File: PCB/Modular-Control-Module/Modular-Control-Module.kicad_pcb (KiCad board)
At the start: 4 copper layers, 59 x 49.4 mm, 29 parts, among them J1 Conn_01x04, SW1 TL3330AF260QG, SW2 TL3330AF260QG, U1 TEMPLATE, U2 RP2040, X1 ABM8G-12.000MHZ-18-D2Y-T

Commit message: WIP save
WIP save gonna try flipping the MCU around.
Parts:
- added J2: DX07S016JA1R1500, AVR-KiCAD-Lib-Connectors:JAE_DX07S016JA1R1500, B.Cu at (82.8, 74.1)
- added R1: RT0603BRD071ML, AVR-KiCAD-Lib-Resistors:R0603, B.Cu at (79.0, 68.1)
- added R10: RC0402FR-071KL, AVR-KiCAD-Lib-Resistors:R0402, B.Cu at (88.5, 80.0)
- added R11: RC0402FR-071KL, AVR-KiCAD-Lib-Resistors:R0402, B.Cu at (106.9, 80.0)
- added R12: RC0402FR-071KL, AVR-KiCAD-Lib-Resistors:R0402, B.Cu at (125.5, 80.0)
- added R4: RC0402FR-075K1L, AVR-KiCAD-Lib-Resistors:R0402, B.Cu at (86.0, 72.8)
- added R5: RC0402FR-075K1L, AVR-KiCAD-Lib-Resistors:R0402, B.Cu at (87.4, 77.2)
- added R7: RC0402FR-071KL, AVR-KiCAD-Lib-Resistors:R0402, B.Cu at (125.5, 53.8)
- added R8: RC0402FR-071KL, AVR-KiCAD-Lib-Resistors:R0402, B.Cu at (107.0, 53.8)
- added R9: RC0402FR-071KL, AVR-KiCAD-Lib-Resistors:R0402, B.Cu at (88.5, 53.8)
- J1: value Conn_01x04 -> Conn_ARM_SWD_TagConnect_TC2030-NL; footprint Connector_PinHeader_2.54mm:PinHeader_1x04_P2.54mm_Vertical -> Connector:Tag-Connect_TC2030-IDC-NL_2x03_P1.27mm_Vertical; moved to B.Cu
- SW1, SW2: value TL3330AF260QG -> B3U-1000P; footprint AVR-KiCAD-Lib-Mech-Switches:SW_TL3330AF260QG -> AVR-KiCAD-Lib-Mech-Switches:B3U-1000P; moved to B.Cu
- moved J1 44.3 mm to (112.4, 75.8), turned to 180 degrees
- moved C14 28.4 mm to (98.2, 67.9), turned to -90 degrees
- moved C8 23.3 mm to (93.7, 69.0), turned to 0 degrees
- moved C11 18.4 mm to (88.0, 73.3), turned to 0 degrees
- moved SW2 16.8 mm to (79.2, 83.7)
- moved SW1 11.7 mm to (79.2, 64.0)
- moved C13 7.88 mm to (98.1, 80.2), turned to 90 degrees
- moved C7 5.85 mm to (92.9, 79.2)
- moved C6 2.91 mm to (90.4, 74.8)
- moved C3 2.28 mm to (91.8, 77.4)
- moved C4 2.11 mm to (107.9, 71.2), turned to 90 degrees
- moved X1 1.81 mm to (105.6, 71.8)
- moved C2 1.70 mm to (105.3, 74.5)
- moved C1 0.85 mm to (94.2, 79.3)
- moved C5 0.63 mm to (102.6, 75.0)
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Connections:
- EN2 pad 2: unconnected-(EN2-S2-Pad2) -> GND
- EN3 pad 2: unconnected-(EN3-S2-Pad2) -> GND
- EN6 pad 2: unconnected-(EN6-S2-Pad2) -> GND
- J1 pad 3: GND -> unconnected-(J1-~{RESET}-Pad3)
- U2 pad 12: unconnected-(U2-GPIO9-Pad12) -> /I2C_SDA
- U2 pad 13: unconnected-(U2-GPIO10-Pad13) -> /I2C_SCL
- U2 pad 14: unconnected-(U2-GPIO11-Pad14) -> /SLAVE_IRQ
- U2 pad 15: unconnected-(U2-GPIO12-Pad15) -> /SPI_SCK
- U2 pad 16: unconnected-(U2-GPIO13-Pad16) -> /SPI_CS
- U2 pad 17: unconnected-(U2-GPIO14-Pad17) -> /SPI_MISO
- U2 pad 18: unconnected-(U2-GPIO15-Pad18) -> /SPI_MOSI
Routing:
- net /SPI_MOSI: track 0.00 -> 33.4 mm, vias 0 -> 1
- net /SPI_MISO: track 0.00 -> 32.2 mm, vias 0 -> 1
- net /SPI_CS: track 0.00 -> 31.0 mm, vias 0 -> 1
- net /SPI_SCK: track 0.00 -> 30.2 mm, vias 0 -> 1
- net +3.3V: track 0.00 -> 27.7 mm, vias 0 -> 15
- net Net-(U2-RUN): track 0.00 -> 27.5 mm, vias 0 -> 2
- net /I2C_SDA: track 0.00 -> 26.1 mm, vias 0 -> 1
- net /SLAVE_IRQ: track 0.00 -> 25.9 mm, vias 0 -> 1
- net /I2C_SCL: track 0.00 -> 25.8 mm, vias 0 -> 1
- net /SWD: track 0.00 -> 22.5 mm
- net GND: track 0.00 -> 19.7 mm, vias 0 -> 21
- net +1V1: track 0.00 -> 18.0 mm
- net /SWCLK: track 0.00 -> 14.7 mm
- net /USB_DM: track 0.00 -> 14.2 mm
- net /USB_DP: track 0.00 -> 13.0 mm
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- added copper zone on B.Cu, net /SH
- added copper zone on F.Cu, net /SH

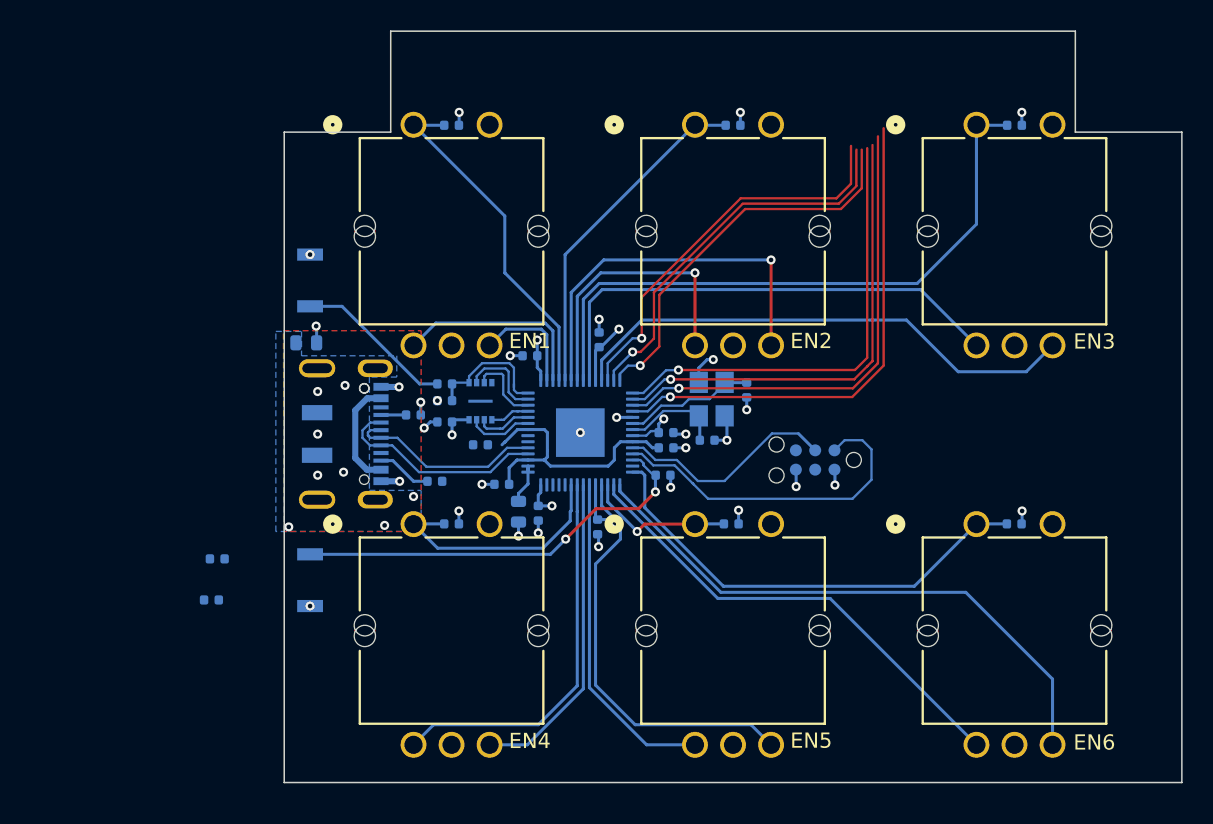
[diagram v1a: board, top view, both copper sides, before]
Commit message: Flip Worked
Flipping MCU 90 degrees worked, PCB redesigned around that topology, connector for main board added.
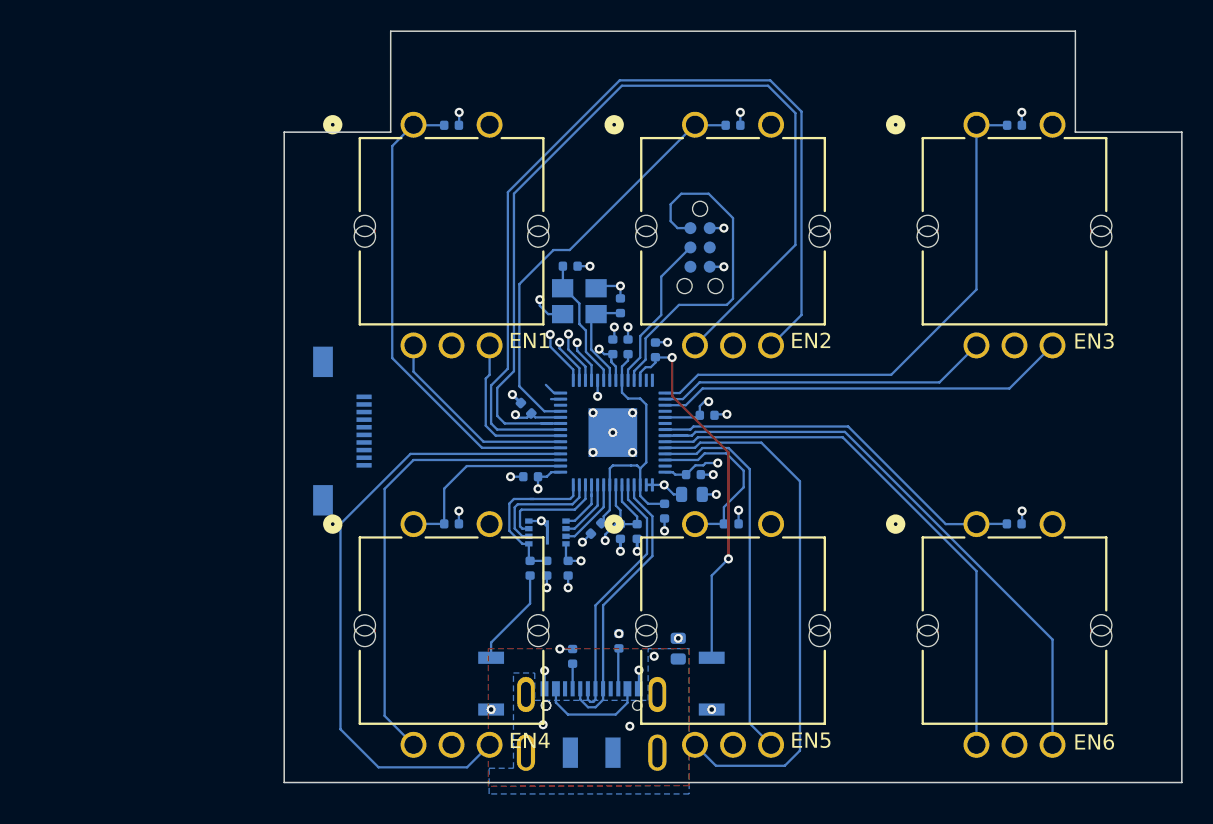
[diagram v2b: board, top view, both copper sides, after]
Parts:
- added T1: 5051101092, AVR-KiCAD-Lib-Connectors:CON_5051101092_MOL, B.Cu at (80.3, 73.9)
- moved R1 31.7 mm to (103.4, 88.2), turned to 90 degrees
- moved SW1 29.0 mm to (91.1, 90.5), turned to 90 degrees
- moved C12 28.3 mm to (100.7, 80.5), turned to 90 degrees
- moved SW2 27.3 mm to (105.6, 90.5)
- moved C9 26.6 mm to (99.6, 80.5), turned to 90 degrees
- moved J2 23.3 mm to (97.7, 91.9), turned to 180 degrees
- moved R4 19.0 mm to (96.5, 88.7), turned to 90 degrees
- moved R5 16.0 mm to (99.5, 87.7), turned to 90 degrees
- moved J1 15.9 mm to (104.8, 61.8), turned to -90 degrees
- moved C4 14.2 mm to (96.3, 63.1), turned to 180 degrees
- moved R2 13.3 mm to (93.7, 82.9), turned to 90 degrees
- moved R3 12.9 mm to (94.8, 82.9), turned to -90 degrees
- moved C11 12.6 mm to (96.2, 82.9), turned to 90 degrees
- moved C7 11.5 mm to (104.3, 78.1), turned to 180 degrees
- moved C3 10.8 mm to (102.5, 79.2), turned to 90 degrees
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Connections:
- U2 pad 11: /EN3_B -> /EN2_S1
- U2 pad 2: /EN1_B -> /EN4_S1
- U2 pad 28: /EN6_S1 -> unconnected-(U2-GPIO17-Pad28)
- U2 pad 29: /EN6_B -> /EN3_S1
- U2 pad 3: /EN1_A -> /EN4_A
- U2 pad 30: /EN6_A -> /EN3_A
- U2 pad 31: /EN5_S1 -> /EN3_B
- U2 pad 32: /EN5_B -> unconnected-(U2-GPIO21-Pad32)
- U2 pad 34: /EN5_A -> unconnected-(U2-GPIO22-Pad34)
- U2 pad 35: /EN4_B -> /EN6_S1
- U2 pad 36: /EN4_A -> /EN6_B
- U2 pad 37: /EN4_S1 -> /EN6_A
- U2 pad 38: unconnected-(U2-GPIO26_ADC0-Pad38) -> /EN5_A
- U2 pad 39: unconnected-(U2-GPIO27_ADC1-Pad39) -> /EN5_B
- U2 pad 4: /EN1_S1 -> /EN4_B
- U2 pad 40: unconnected-(U2-GPIO28_ADC2-Pad40) -> /EN5_S1
- U2 pad 5: /EN2_S1 -> /EN1_S1
- U2 pad 6: /EN2_B -> /EN1_A
- U2 pad 7: /EN2_A -> /EN1_B
- U2 pad 8: /EN3_S1 -> /EN2_B
- U2 pad 9: /EN3_A -> /EN2_A
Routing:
- net /EN2_A: track 18.7 -> 60.3 mm, vias 1 -> 0
- net /EN2_B: track 25.4 -> 59.8 mm, vias 1 -> 0
- net /SPI_MOSI: track 33.4 -> 2.88 mm
- net /SPI_MISO: track 32.2 -> 3.50 mm
- net /SPI_CS: track 31.0 -> 3.04 mm
- net /SPI_SCK: track 30.2 -> 3.64 mm
- net /I2C_SDA: track 26.1 -> 0.00 mm, vias 1 -> 0
- net /I2C_SCL: track 25.8 -> 0.62 mm, vias 1 -> 0
- net /SLAVE_IRQ: track 25.9 -> 1.19 mm, vias 1 -> 0
- net /EN4_B: track 21.1 -> 41.3 mm
- net /EN5_A: track 21.8 -> 35.6 mm
- net /EN3_A: track 32.4 -> 21.9 mm
- net +3.3V: track 27.7 -> 37.3 mm, vias 15 -> 17
- net /EN1_S1: track 22.8 -> 31.4 mm
- net /EN3_B: track 34.2 -> 27.1 mm
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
